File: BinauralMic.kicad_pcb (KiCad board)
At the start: 4 copper layers, 58 x 63.8 mm, 58 parts, among them IC1 PCM2903CDBR, J2 USB4105-GF-A-120, J3 Conn_01x02_Pin, J4 Conn_01x02_Pin, U1 MIC5504-3.3YM5, U2 TL972QDRQ1, U3 74LVC1G08, Y1 ABLS-12.000MHZ-20-D-3-H-T

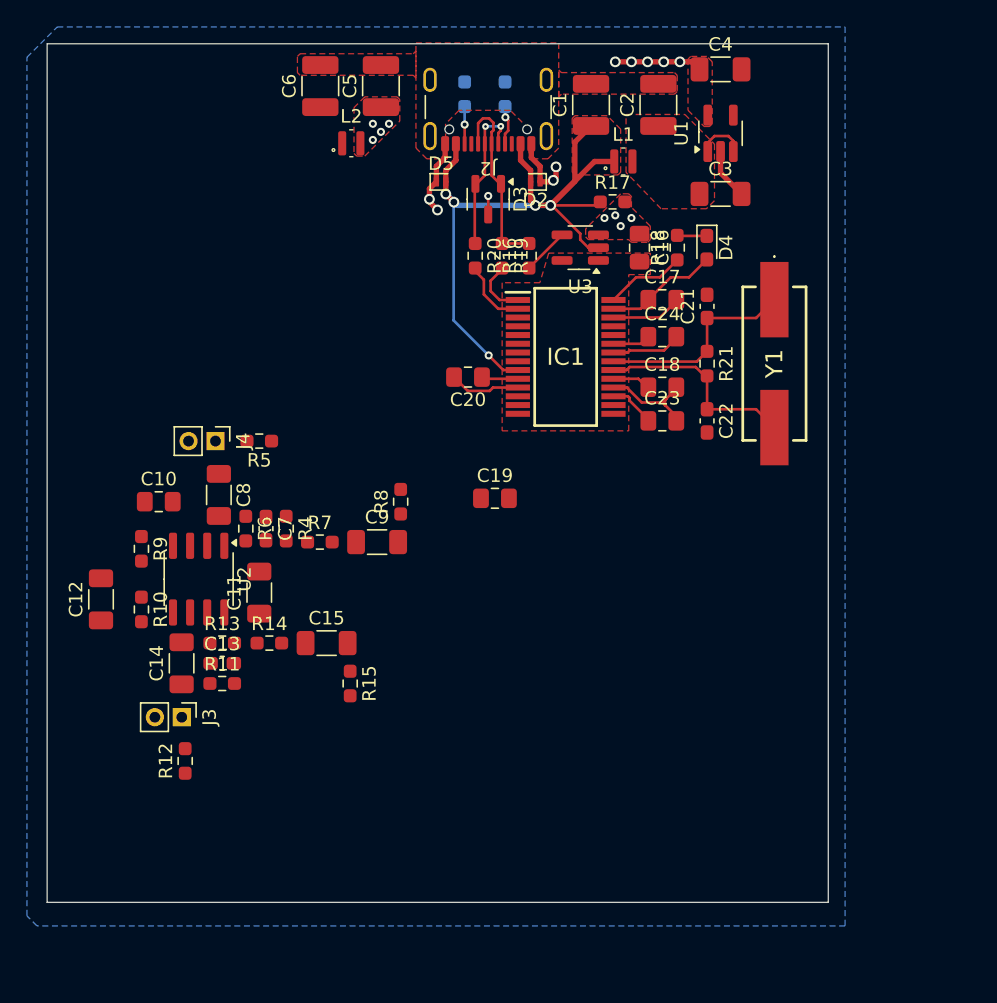
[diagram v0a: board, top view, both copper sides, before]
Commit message: Flipped inductor direction (dot towards EMI) and shuffled some components around
Hopefully a more rested me can fit this jigsaw a little better
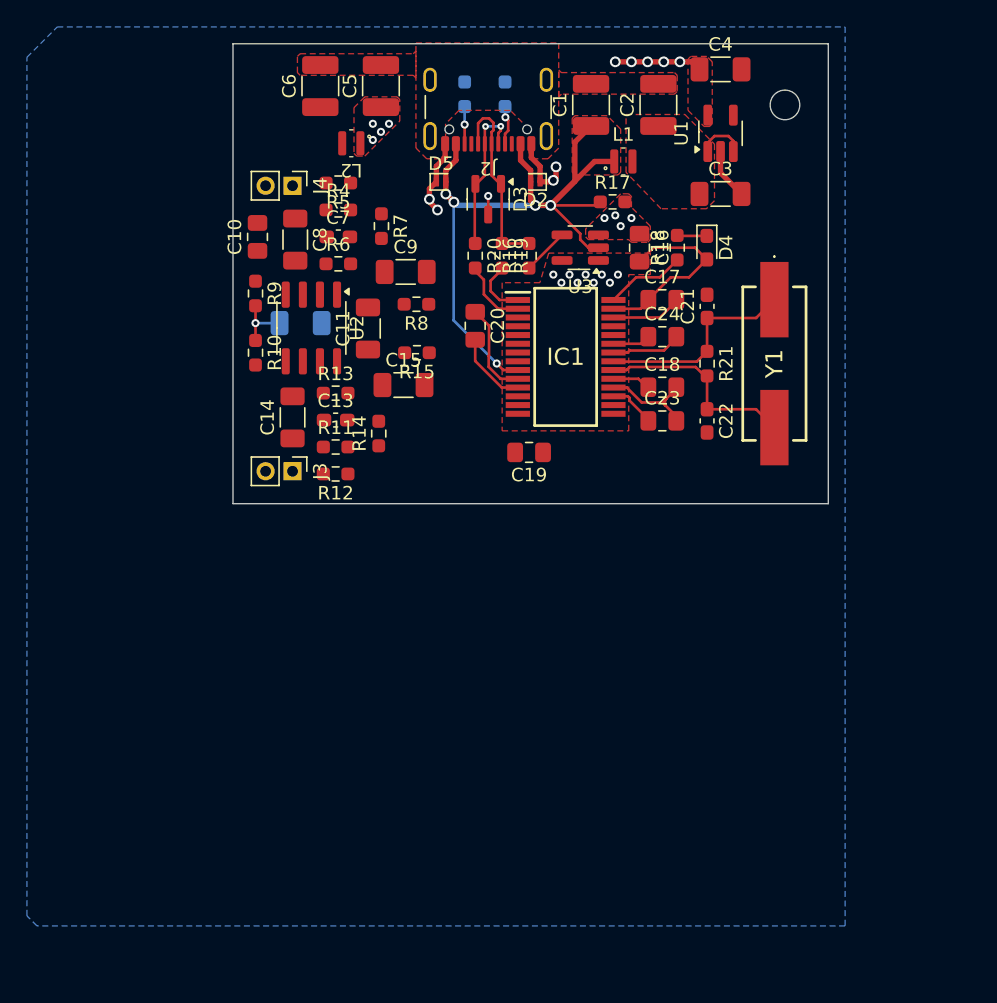
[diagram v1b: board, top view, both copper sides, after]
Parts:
- added REF**: MountingHole_2.2mm_M2, MountingHole:MountingHole_2.2mm_M2, F.Cu at (162.6, 55.6)
- C12: moved to B.Cu
- moved C12 25.3 mm to (126.6, 71.8), turned to 180 degrees
- moved R15 25.1 mm to (135.3, 74.0), turned to 180 degrees
- moved R12 24.1 mm to (129.2, 83.0), turned to 180 degrees
- moved R4 24.0 mm to (129.4, 63.4), turned to 0 degrees
- moved R7 23.9 mm to (132.6, 64.6), turned to -90 degrees
- moved C7 22.3 mm to (129.4, 65.4), turned to 0 degrees
- moved C11 21.2 mm to (131.6, 72.2)
- moved C10 21.0 mm to (123.4, 65.4), turned to 90 degrees
- moved R10 20.9 mm to (123.3, 74.0)
- moved R6 20.8 mm to (129.4, 67.4), turned to 0 degrees
- moved R9 20.8 mm to (123.3, 69.6)
- moved U2 20.4 mm to (127.4, 72.2)
- moved R13 20.4 mm to (129.2, 77.0)
- moved C9 20.2 mm to (134.4, 68.0)
- moved R5 20.0 mm to (129.4, 61.4)
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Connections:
- L2 pad 1: +3.3VA -> VCC
- L2 pad 2: VCC -> +3.3VA
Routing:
- net VCC: track 27.0 -> 37.1 mm, vias 9 -> 18
- net /VCOM: track 0.00 -> 4.36 mm, vias 0 -> 1
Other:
- board size 58 x 63.8 mm -> 44.2 x 34.2 mm

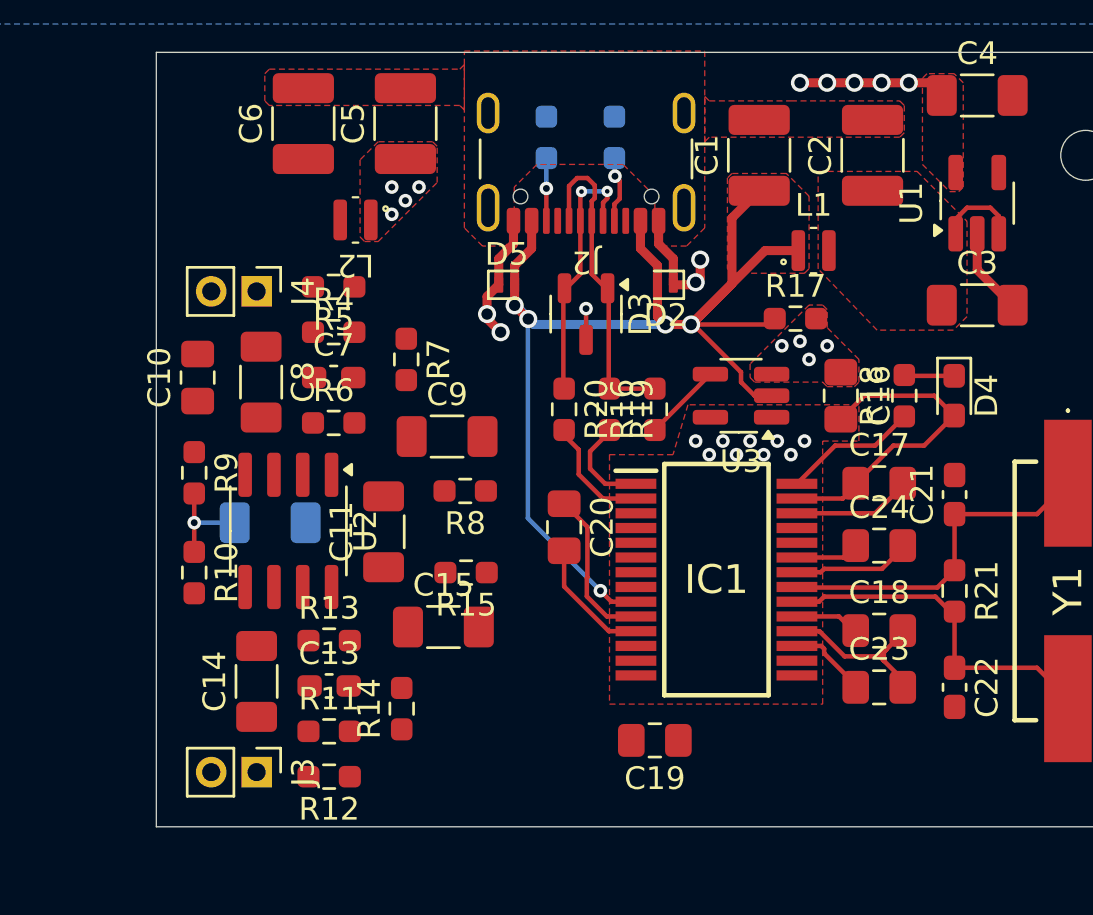
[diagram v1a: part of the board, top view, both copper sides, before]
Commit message: Layout + routing for preamp
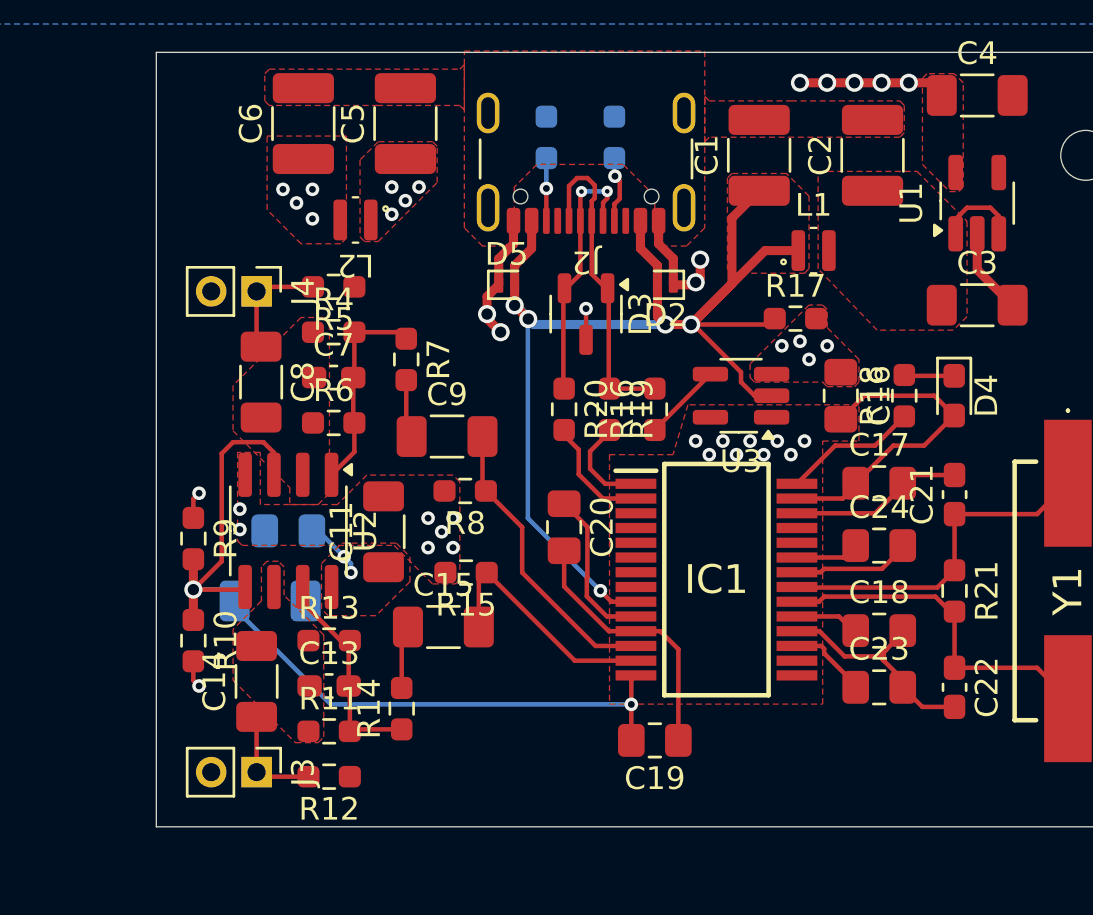
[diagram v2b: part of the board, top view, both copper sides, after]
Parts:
- C10: moved to B.Cu
- moved C10 7.86 mm to (127.4, 72.2), turned to 180 degrees
- moved C12 3.45 mm to (126.6, 75.2)
- moved R10 3.00 mm to (123.2, 77.0)
- moved R9 2.90 mm to (123.2, 72.5)
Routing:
- net /VCOM: track 4.36 -> 62.9 mm, vias 1 -> 2
- net /VIN_{L}: track 0.00 -> 13.1 mm
- net GND: track 39.7 -> 52.2 mm, vias 9 -> 17
- net /VIN_{R}: track 0.00 -> 10.7 mm
- net /Mic Preamp/VOUT_{R}: track 0.00 -> 9.82 mm
- net /Mic Preamp/VOUT_{L}: track 0.00 -> 9.15 mm
- net /VRAW_{L}: track 0.00 -> 5.09 mm
- net /VRAW_{R}: track 0.00 -> 4.81 mm
- net +3.3VA: track 0.00 -> 3.91 mm, vias 0 -> 7
- net /Mic Preamp/VOUT_{R}_R: track 0.00 -> 2.80 mm
- net /Mic Preamp/VOUT_{L}_R: track 0.00 -> 2.59 mm
- added copper zone on F.Cu, net +3.3VA
- added copper zone on In2.Cu, net +3.3VA
- added copper zone on F.Cu, net /Mic Preamp/VN_{L}
- added copper zone on F.Cu, net /Mic Preamp/VN_{R}
- added copper zone on In2.Cu, net GND

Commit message: Finished routing
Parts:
- added G***: LOGO, LOGO, B.Cu at (159.8, 73.0)
- added G***: LOGO, LOGO, B.Cu at (163.4, 73.0)
- added REF**: MountingHole_2.2mm_M2, MountingHole:MountingHole_2.2mm_M2, F.Cu at (123.6, 54.2)
- added REF**: MountingHole_2.2mm_M2, MountingHole:MountingHole_2.2mm_M2, F.Cu at (138.4, 82.4)
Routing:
- net +5V: track 3.69 -> 55.9 mm, vias 0 -> 4
- net +3.3VA: track 3.91 -> 3.99 mm, vias 7 -> 11
- net GND: vias 17 -> 132
- added copper zone on F.Cu, net /VCOM
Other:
- board size 44.2 x 34.2 mm -> 45 x 34.2 mm
- board text added: "LEFT"
- board text added: "LeftistTachyon, 2024"
- board text added: "Preamp"
- board text added: "RIGHT"
- board text added: "USB C Port"
- board text added: "凹凸"

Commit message: Passing review from @MorrisYLin
Thank you for looking everything over!
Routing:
- net GND: vias 132 -> 131
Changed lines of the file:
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@@
-	)
-	(via
-		(at 134.6 78.4)
-		(size 0.6)
-		(drill 0.3)
-		(layers "F.Cu" "B.Cu")
-		(free yes)
-		(net 2)
 	)
 	(via

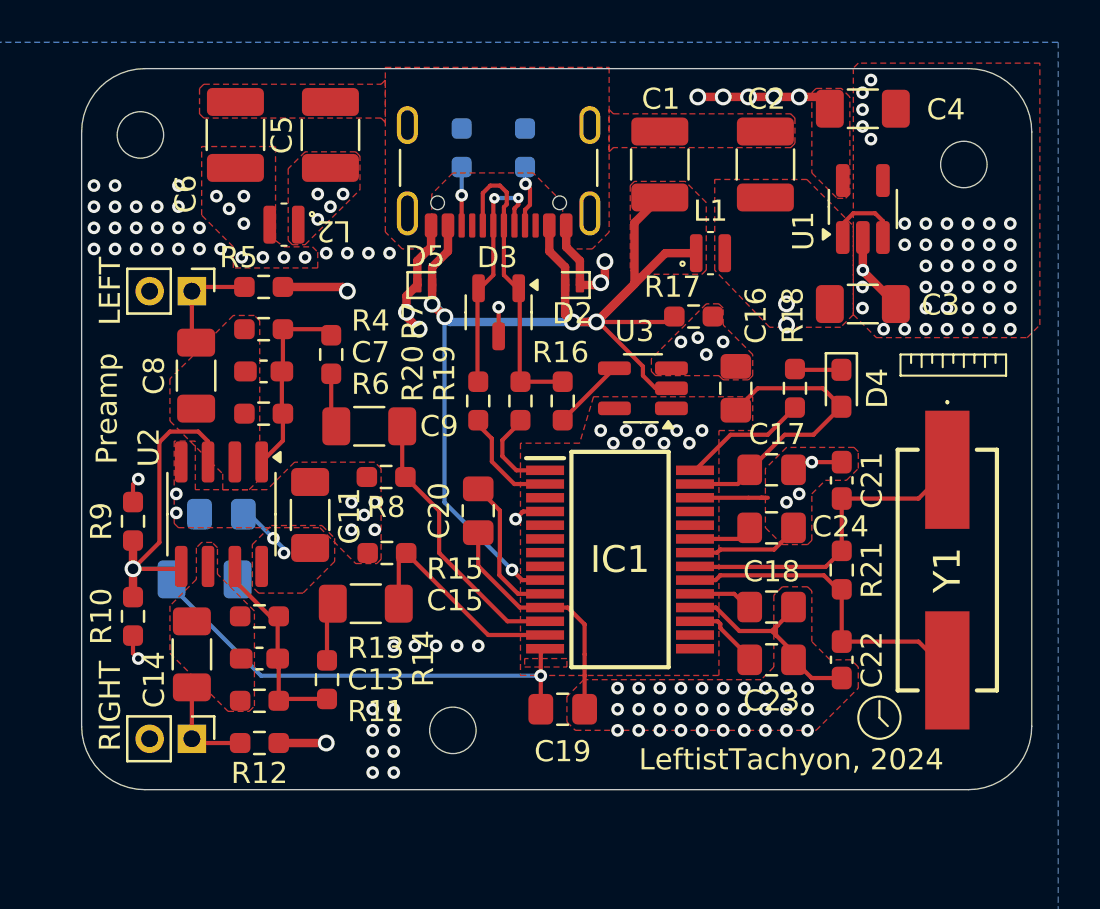
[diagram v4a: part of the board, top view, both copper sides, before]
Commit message: Add silkscreen + some bonus test points
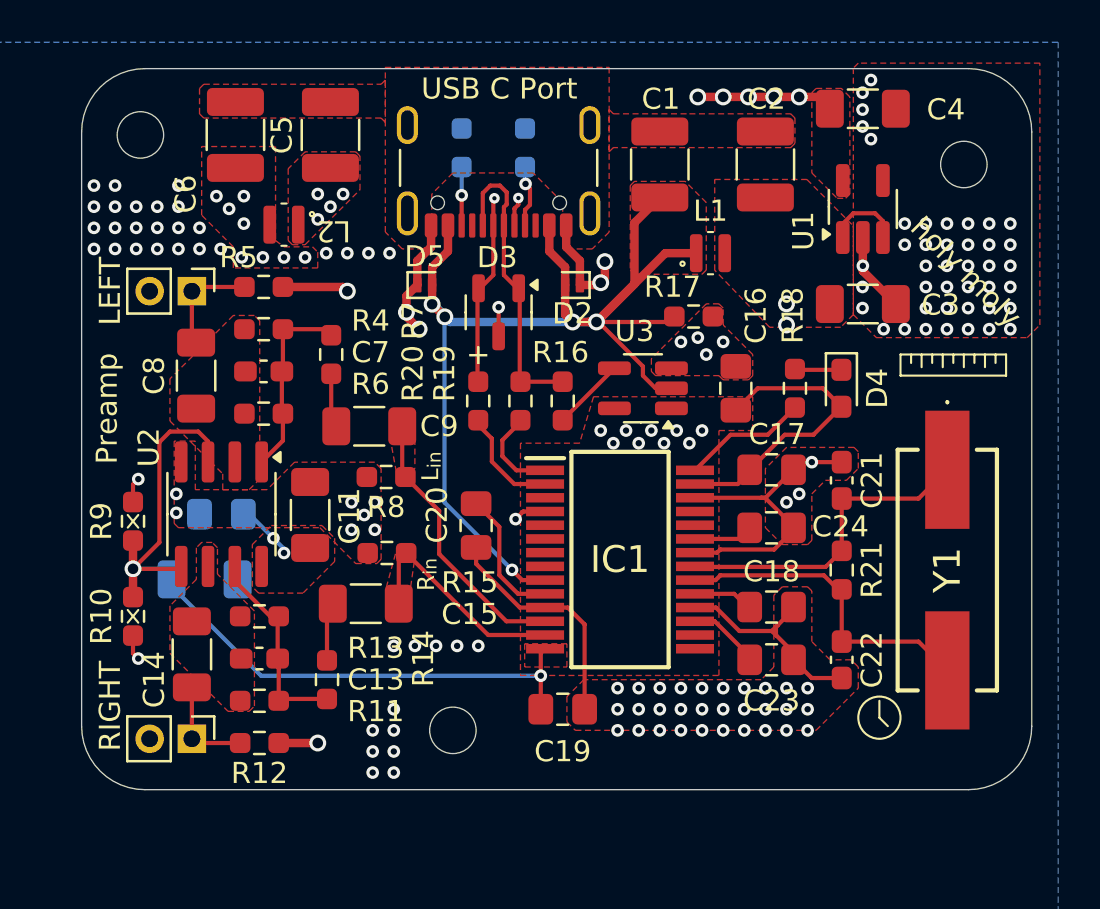
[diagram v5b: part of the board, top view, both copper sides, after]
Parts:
- added G***: LOGO, LOGO, B.Cu at (130.4, 53.1)
- added G***: LOGO, LOGO, B.Cu at (151.8, 54.6)
- added G***: LOGO, LOGO, B.Cu at (161.4, 56.8)
- added G***: LOGO, LOGO, B.Cu at (153.8, 82.8)
- added G***: LOGO, LOGO, B.Cu at (133.7, 72.4)
- added G***: LOGO, LOGO, B.Cu at (155.6, 66.0)
- moved C20 0.71 mm to (139.5, 72.7)
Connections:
- net /USB ADC/D+_R renamed /USB ADC/D_R+
- net /USB ADC/D-_R renamed /USB ADC/D_R-
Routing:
- net +5V: track 55.9 -> 62.6 mm
- net GND: track 52.2 -> 55.2 mm, vias 131 -> 130
- net VCC: track 37.1 -> 36.3 mm
- added copper zone on F.Cu, net /VIN_{L}
- added copper zone on F.Cu, net /VIN_{R}
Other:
- board text added: "+"
- board text added: "BINAURAL MICROPHONE"
- board text added: "Based on the PCM2903C"
- board text added: "Besties"
- board text added: "Contact @leftisttachyon for support"
- board text added: "JJJJJJJJ"
- board text added: "L_{in}"
- board text added: "R_{in}"
- board text added: "Source: @unenemiko"
- board text added: "Special thanks to: MorrisYLin for reviewing the board Noccant for the funding"
- board text added: "^{+}LEFT^{-}"
- board text added: "_{+}RIGHT_{-}"
- board text added: "holy moly"
- board text added: "https://github.com/ LeftistTachyon/BinauralMic"
- board text added: "the"

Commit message: Ordered!
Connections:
- J2 pad S1: GND -> unconnected-(J2-SHIELD-PadS1)_3
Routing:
- net /D+: track 14.3 -> 12.1 mm
- net GND: vias 130 -> 139
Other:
- board text added: "JLCJLCJLCJLC"
